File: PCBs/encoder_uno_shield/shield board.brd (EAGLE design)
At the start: 66.4 x 53.1 mm, 11 parts, among them U1 ARDUINOR3-BPLACE

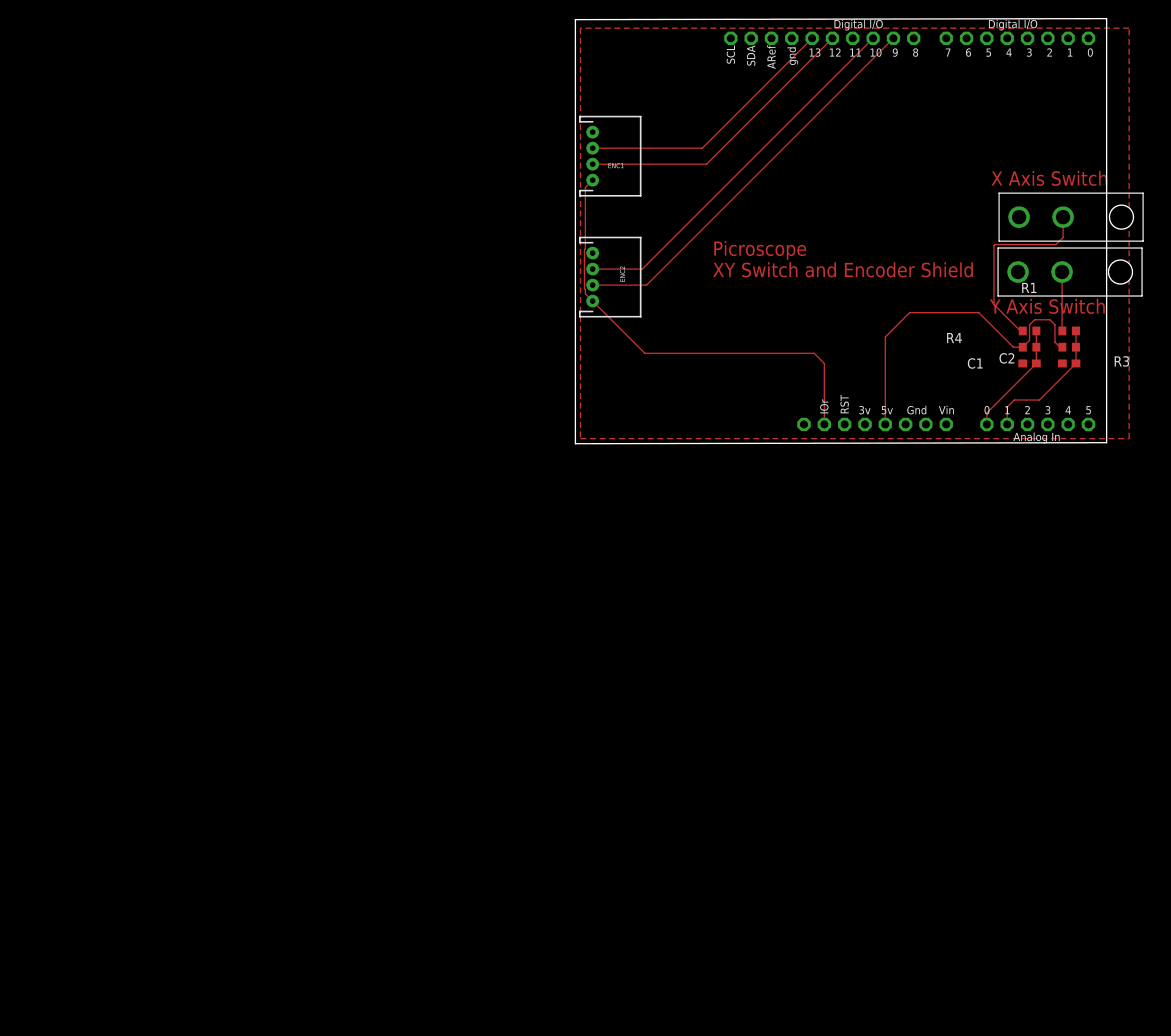
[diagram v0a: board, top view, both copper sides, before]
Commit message: added debounce to sch, about to delete and add back as design block
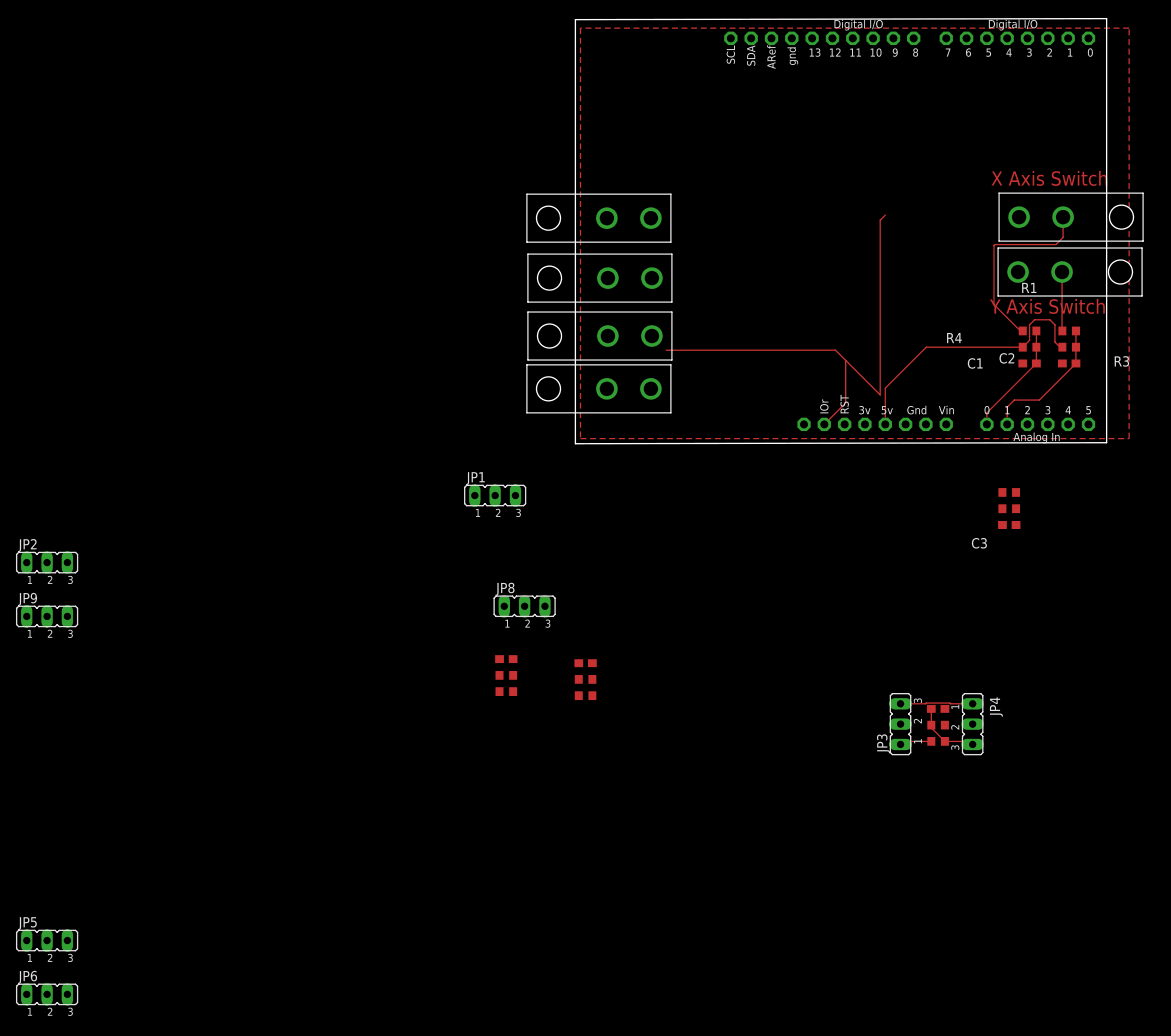
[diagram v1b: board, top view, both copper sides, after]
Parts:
- removed ENC1, ENC2: (no value), SparkFun-Connectors:JST-4-PTH
- added C3, C4, C5, C6: 0.1uF, adafruit:C0603
- added JP1, JP2, JP3, JP4, JP5, JP6, JP8, JP9: (no value), jumper:JP2
- added R10, R12, R6, R8: 10k, resistor:R0603
- added R11, R5, R7, R9: 1k, resistor:R0603
- added U$3, U$4, U$5, U$6: MOLEX_0039301022, pat:MINI-FIT_JR_CONN
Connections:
- new net E1CHA: JP8.2, U1.D12
- new net E1CHA_BYPASS: JP1.3, JP8.1
- new net E1CHA_DB: C3.1, JP8.3, R5.2, R6.1
- new net E1CHB: JP9.2, U1.D13
- new net E1CHB_BYPASS: JP2.3, JP9.1
- new net E1CHB_DB: C4.1, JP9.3, R7.2, R8.1
- new net E2CHA: JP6.2, U1.D9
- new net E2CHA_BYPASS: JP5.3, JP6.1
- new net E2CHA_DB: C6.1, JP6.3, R11.2, R12.1
- new net E2CHB: JP4.2, U1.D10
- new net E2CHB_BYPASS: JP3.3, JP4.1
- new net E2CHB_DB: C5.1, JP4.3, R10.1, R9.2
- new net N$2: JP1.1, R5.1
- new net N$3: JP2.1, R7.1
- new net N$5: JP3.1, R9.1
- new net N$6: JP5.1, R11.1
- net E1CHA_RAW: now also JP1.2, U$5.P$2; no longer ENC1.3, U1.D12
- net E1CHB_RAW: now also JP2.2, U$5.P$1; no longer ENC1.2, U1.D13
- net E2CHA_RAW: now also JP5.2, U$6.P$2; no longer ENC2.3, U1.D9
- net E2CHB_RAW: now also JP3.2, U$6.P$1; no longer ENC2.2, U1.D10
- net GND: now also C3.2, C4.2, C5.2, C6.2, U$3.P$1, U$4.P$1; no longer ENC1.1, ENC2.1
- net VCC: now also R10.2, R12.2, R6.2, R8.2, U$3.P$2, U$4.P$2; no longer ENC1.4, ENC2.4
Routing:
- net E2CHA_RAW: track 50.4 -> 0.00 mm
- net E2CHB_RAW: track 47.0 -> 0.00 mm
- net E1CHA_RAW: track 36.8 -> 0.00 mm
- net E1CHB_RAW: track 33.1 -> 0.00 mm
- net E2CHB_BYPASS: track 0.00 -> 9.09 mm
- net E2CHB_DB: track 0.00 -> 8.39 mm
- net N$5: track 0.00 -> 4.01 mm
- net VCC: track 97.5 -> 95.3 mm
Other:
- board text removed: "Picroscope XY Switch and Encoder Shield"

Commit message: jumper togglable debounce circuit added for encoders
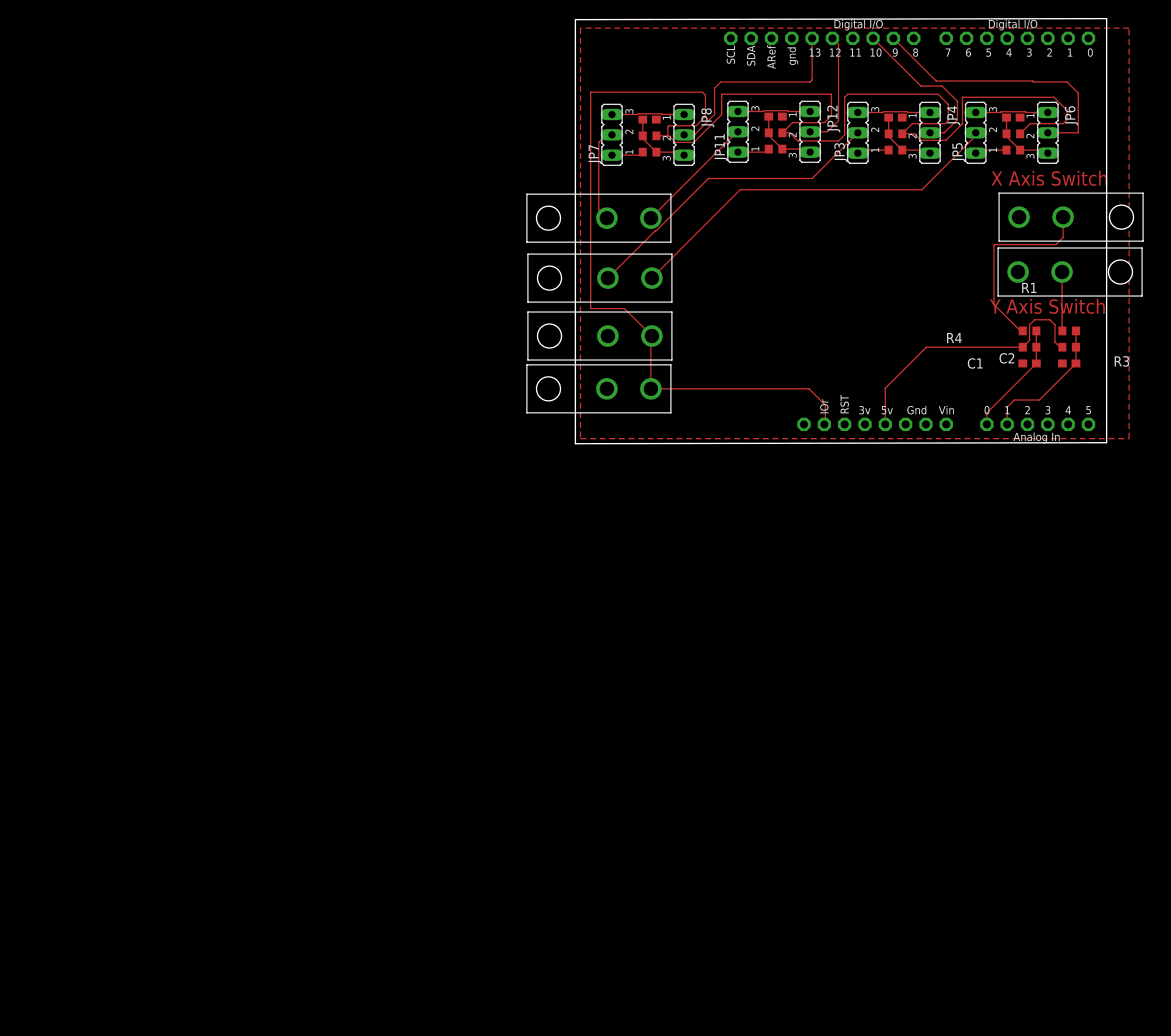
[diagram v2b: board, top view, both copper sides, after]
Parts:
- removed C3: 0.1uF, adafruit:C0603
- removed JP1, JP2, JP9: (no value), jumper:JP2
- removed R5: 1k, resistor:R0603
- removed R6: 10k, resistor:R0603
- added C8: 0.1uF, adafruit:C0603
- added JP11, JP12, JP7: (no value), jumper:JP2
- added R15: 1k, resistor:R0603
- added R16: 10k, resistor:R0603
- moved JP6 165.1 mm to (58.4, 39.0), turned to 270 degrees
- moved JP5 153.8 mm to (49.4, 39.0), turned to 90 degrees
- moved C4 86.7 mm to (54.1, 40.9)
- moved R7 86.7 mm to (54.1, 36.8), turned to 0 degrees
- moved R8 86.7 mm to (54.1, 38.9)
- moved C5 74.1 mm to (39.4, 40.9)
- moved R10 74.1 mm to (39.4, 38.9)
- moved R9 74.1 mm to (39.4, 36.8)
- moved JP3 74.1 mm to (34.7, 39.0)
- moved JP4 74.1 mm to (43.7, 39.0)
- moved C6 69.8 mm to (8.64, 40.6)
- moved R11 69.8 mm to (8.64, 36.6), turned to 0 degrees
- moved R12 69.8 mm to (8.64, 38.6)
- moved JP8 62.2 mm to (13.0, 38.7), turned to 270 degrees
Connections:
- removed net N$2: JP1.1, R5.1
- new net N$8: JP11.1, R15.1
- net E1CHA: now also JP12.2; no longer JP8.2
- net E1CHA_BYPASS: now also JP11.3, JP12.1; no longer JP1.3, JP8.1
- net E1CHA_DB: now also C8.1, JP12.3, R15.2, R16.1; no longer C3.1, JP8.3, R5.2, R6.1
- net E1CHA_RAW: now also JP11.2; no longer JP1.2
- net E1CHB: now also JP8.2; no longer JP9.2
- net E1CHB_BYPASS: now also JP7.3, JP8.1; no longer JP2.3, JP9.1
- net E1CHB_DB: now also C6.1, JP8.3, R11.2, R12.1; no longer C4.1, JP9.3, R7.2, R8.1
- net E1CHB_RAW: now also JP7.2; no longer JP2.2
- net E2CHA_DB: now also C4.1, R7.2, R8.1; no longer C6.1, R11.2, R12.1
- net GND: now also C8.2; no longer C3.2
- net N$3: now also JP5.1; no longer JP2.1
- net N$6: now also JP7.1; no longer JP5.1
- net VCC: now also R16.2; no longer R6.2
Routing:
- net VCC: track 95.3 -> 231.4 mm
- net E2CHA_RAW: track 0.00 -> 48.2 mm
- net E2CHB_RAW: track 0.00 -> 38.8 mm
- net E2CHA: track 0.00 -> 34.7 mm
- net E1CHB: track 0.00 -> 26.0 mm
- net E2CHB: track 0.00 -> 20.2 mm
- net E1CHA_RAW: track 0.00 -> 15.4 mm
- net E1CHA: track 0.36 -> 15.1 mm
- net E1CHB_RAW: track 0.00 -> 11.9 mm
- net E1CHA_BYPASS: track 0.00 -> 9.09 mm
- net E1CHB_BYPASS: track 0.00 -> 9.09 mm
- net E2CHA_BYPASS: track 0.00 -> 9.09 mm
- net E1CHA_DB: track 0.00 -> 8.39 mm
- net E2CHA_DB: track 0.00 -> 8.39 mm
- net E1CHB_DB: track 0.00 -> 8.39 mm
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
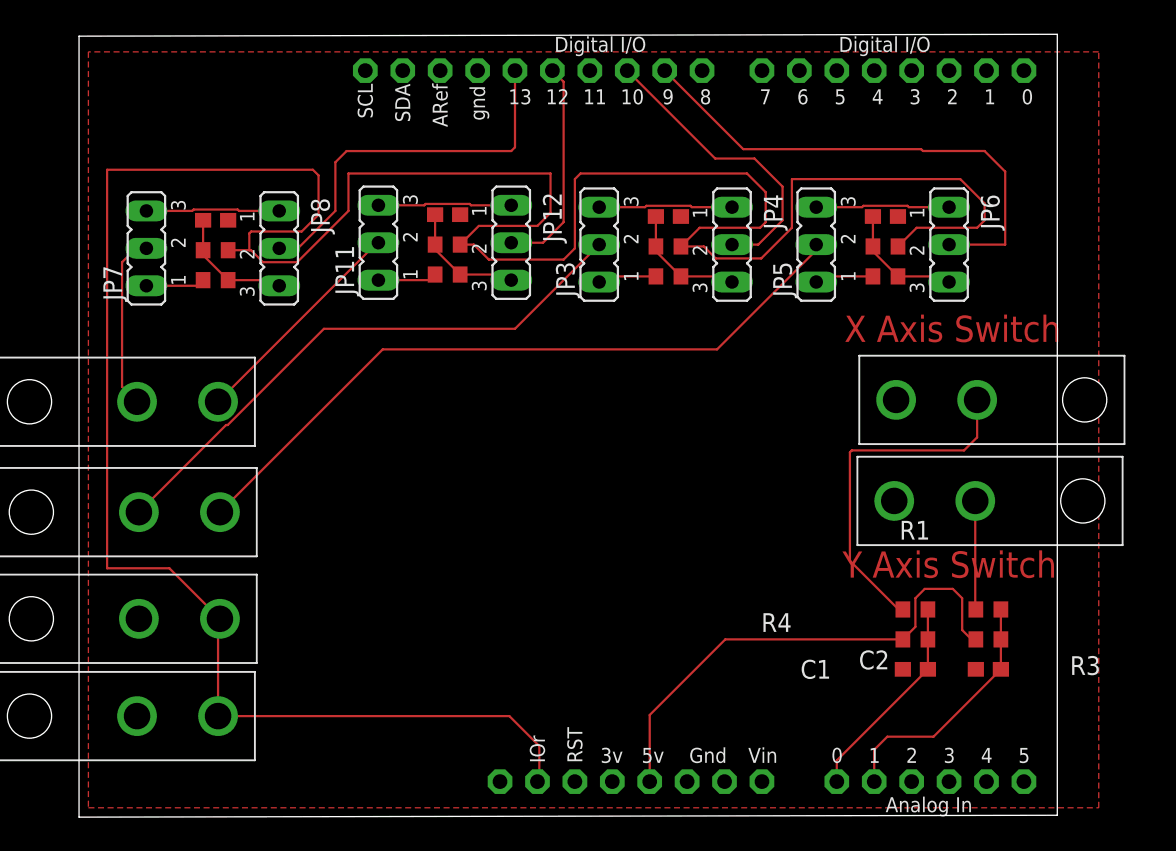
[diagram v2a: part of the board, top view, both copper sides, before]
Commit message: moved components to bottom layer
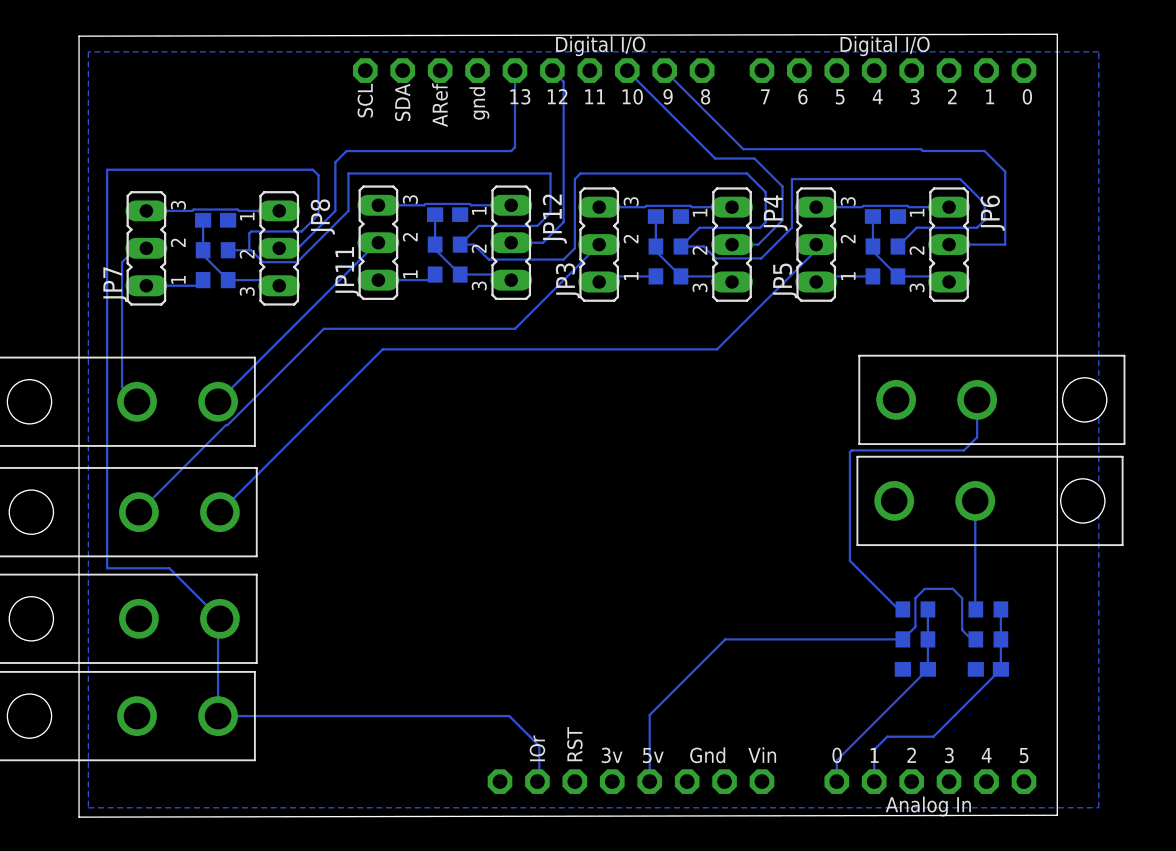
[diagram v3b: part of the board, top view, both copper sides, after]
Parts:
- flipped C1 to the bottom
- flipped C2 to the bottom
- flipped C4 to the bottom
- flipped C5 to the bottom
- flipped C6 to the bottom
- flipped C8 to the bottom
- flipped R1 to the bottom
- flipped R10 to the bottom
- flipped R11 to the bottom
- flipped R12 to the bottom
- flipped R15 to the bottom
- flipped R16 to the bottom
- flipped R2 to the bottom
- flipped R3 to the bottom
- flipped R4 to the bottom
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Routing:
- added copper zone on layer 16, net GND
- removed copper zone on layer 1, net GND
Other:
- board text removed: "X Axis Switch"
- board text removed: "Y Axis Switch"

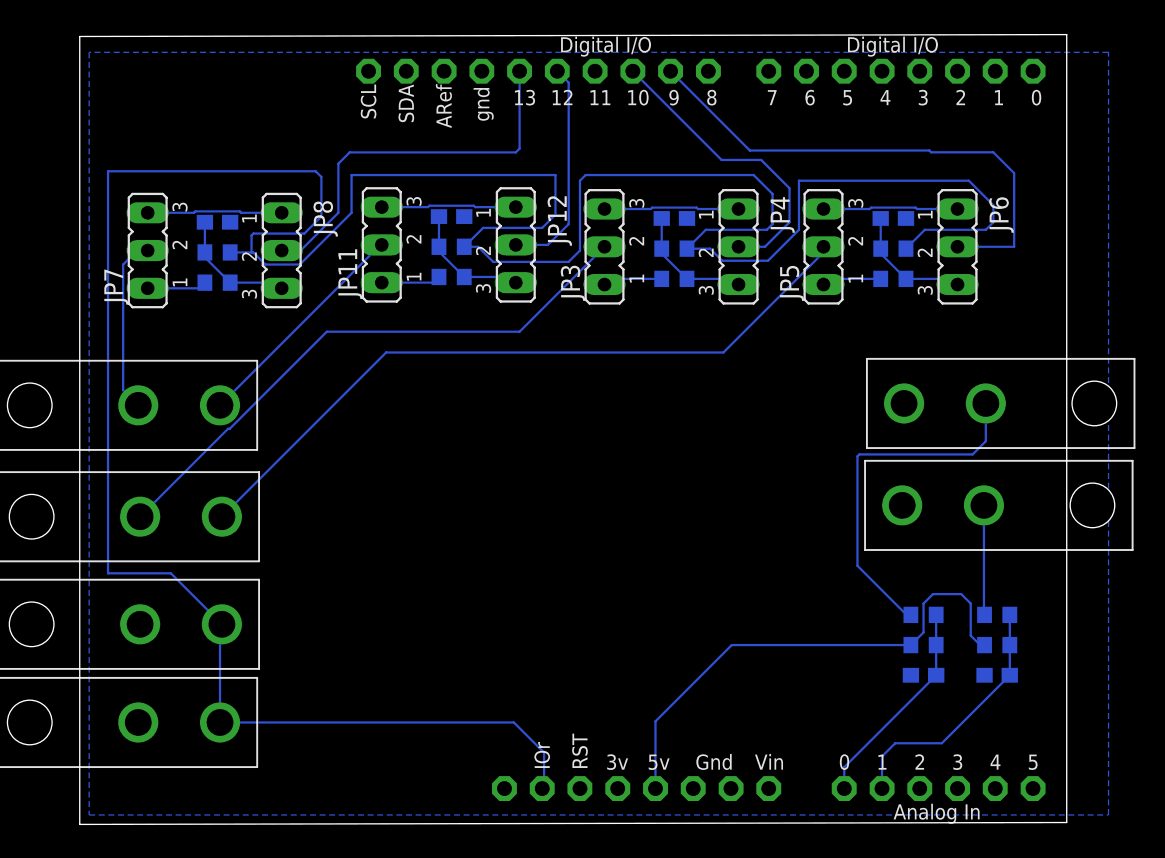
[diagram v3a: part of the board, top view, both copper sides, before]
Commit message: moved components and wires back to top layer
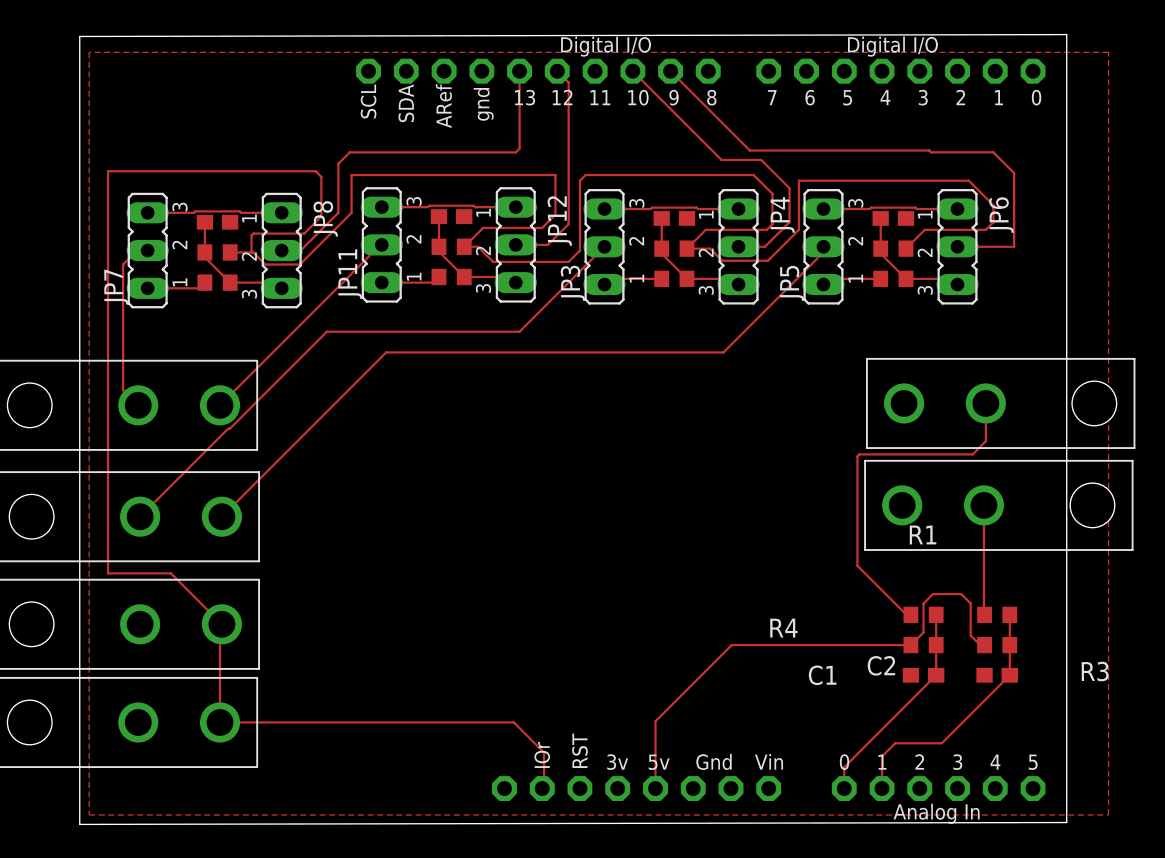
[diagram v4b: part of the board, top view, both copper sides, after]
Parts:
- flipped C1 to the top
- flipped C2 to the top
- flipped C4 to the top
- flipped C5 to the top
- flipped C6 to the top
- flipped C8 to the top
- flipped R1 to the top
- flipped R10 to the top
- flipped R11 to the top
- flipped R12 to the top
- flipped R15 to the top
- flipped R16 to the top
- flipped R2 to the top
- flipped R3 to the top
- flipped R4 to the top
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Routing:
- added copper zone on layer 1, net GND
- removed copper zone on layer 16, net GND
